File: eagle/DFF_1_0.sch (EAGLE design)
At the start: 15 parts, among them IC1 74HC74N, X1 In A, X2 In B, X3 Ctrl, X4 Out X, X5 Out Y

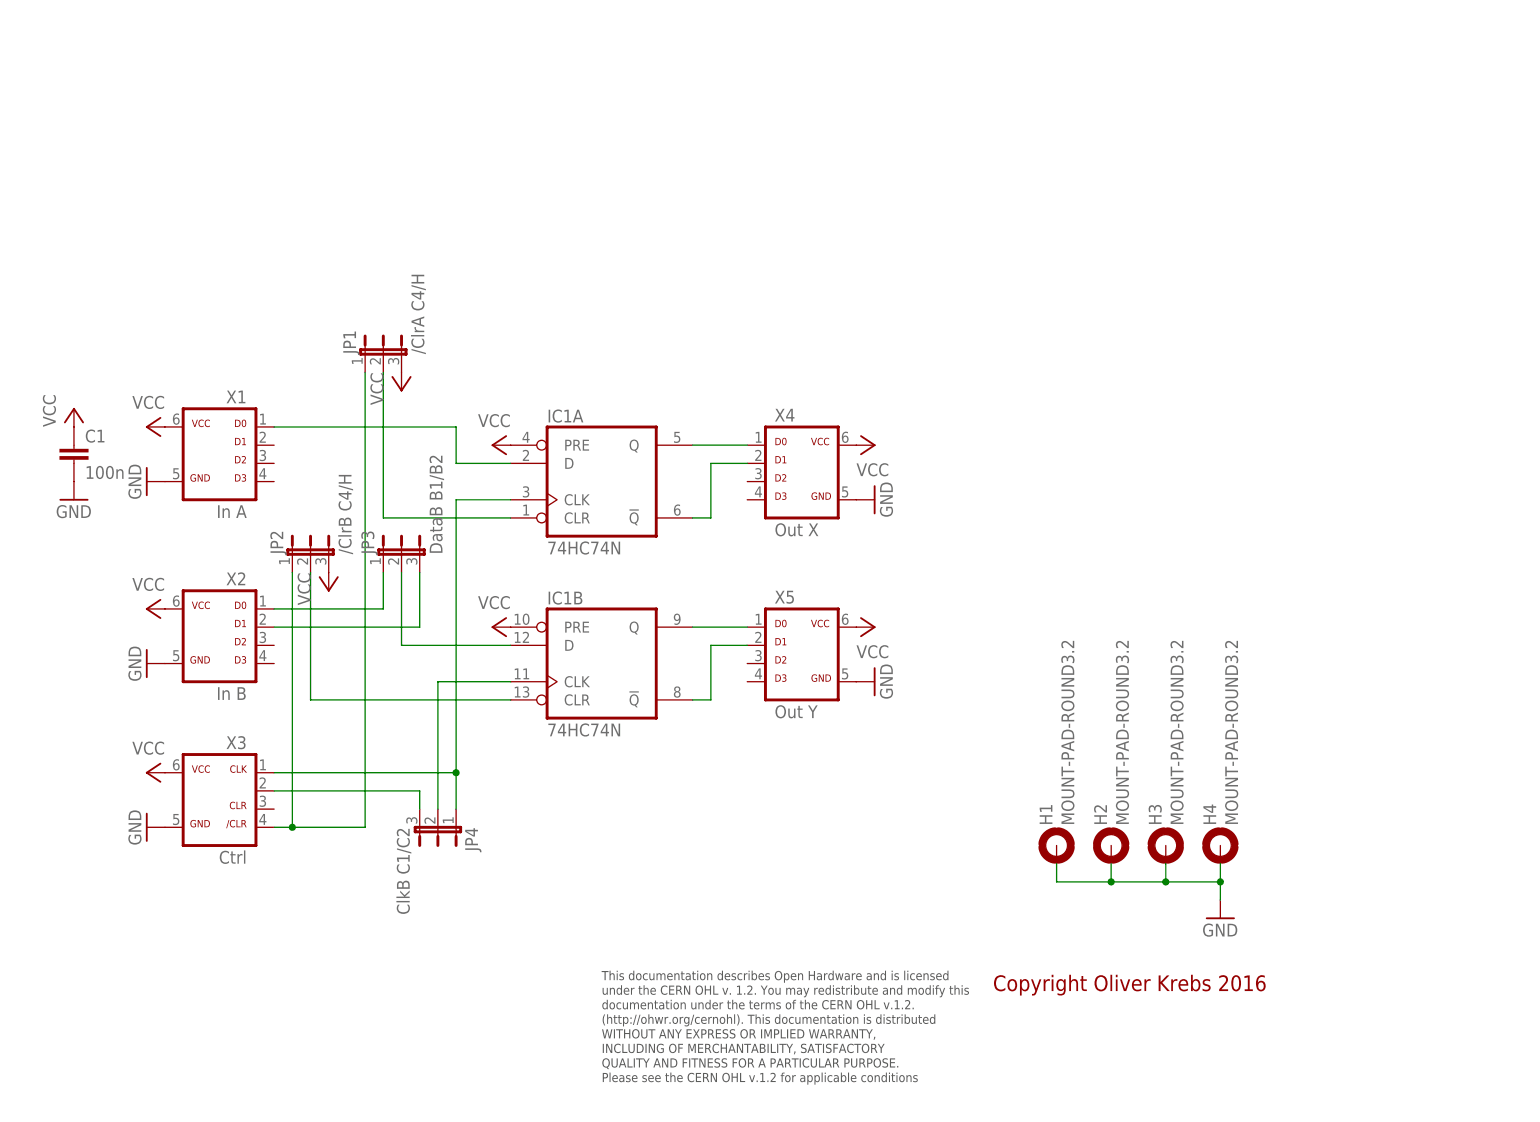
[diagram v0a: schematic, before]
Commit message: Add new tetra-Board and arduino files
Add AMP_1_0, AVC_1_0, D18_1_1, IOP_1_2, MIC_1_0, PIN_1_1, POT_1_0, PWA_1_0, PWR_1_0, RGF 2.0, SOC_2_0, VLT_1_0
Add mex_nano_shield_keyboard, mex_nano_shied_numbers

New arduino projects
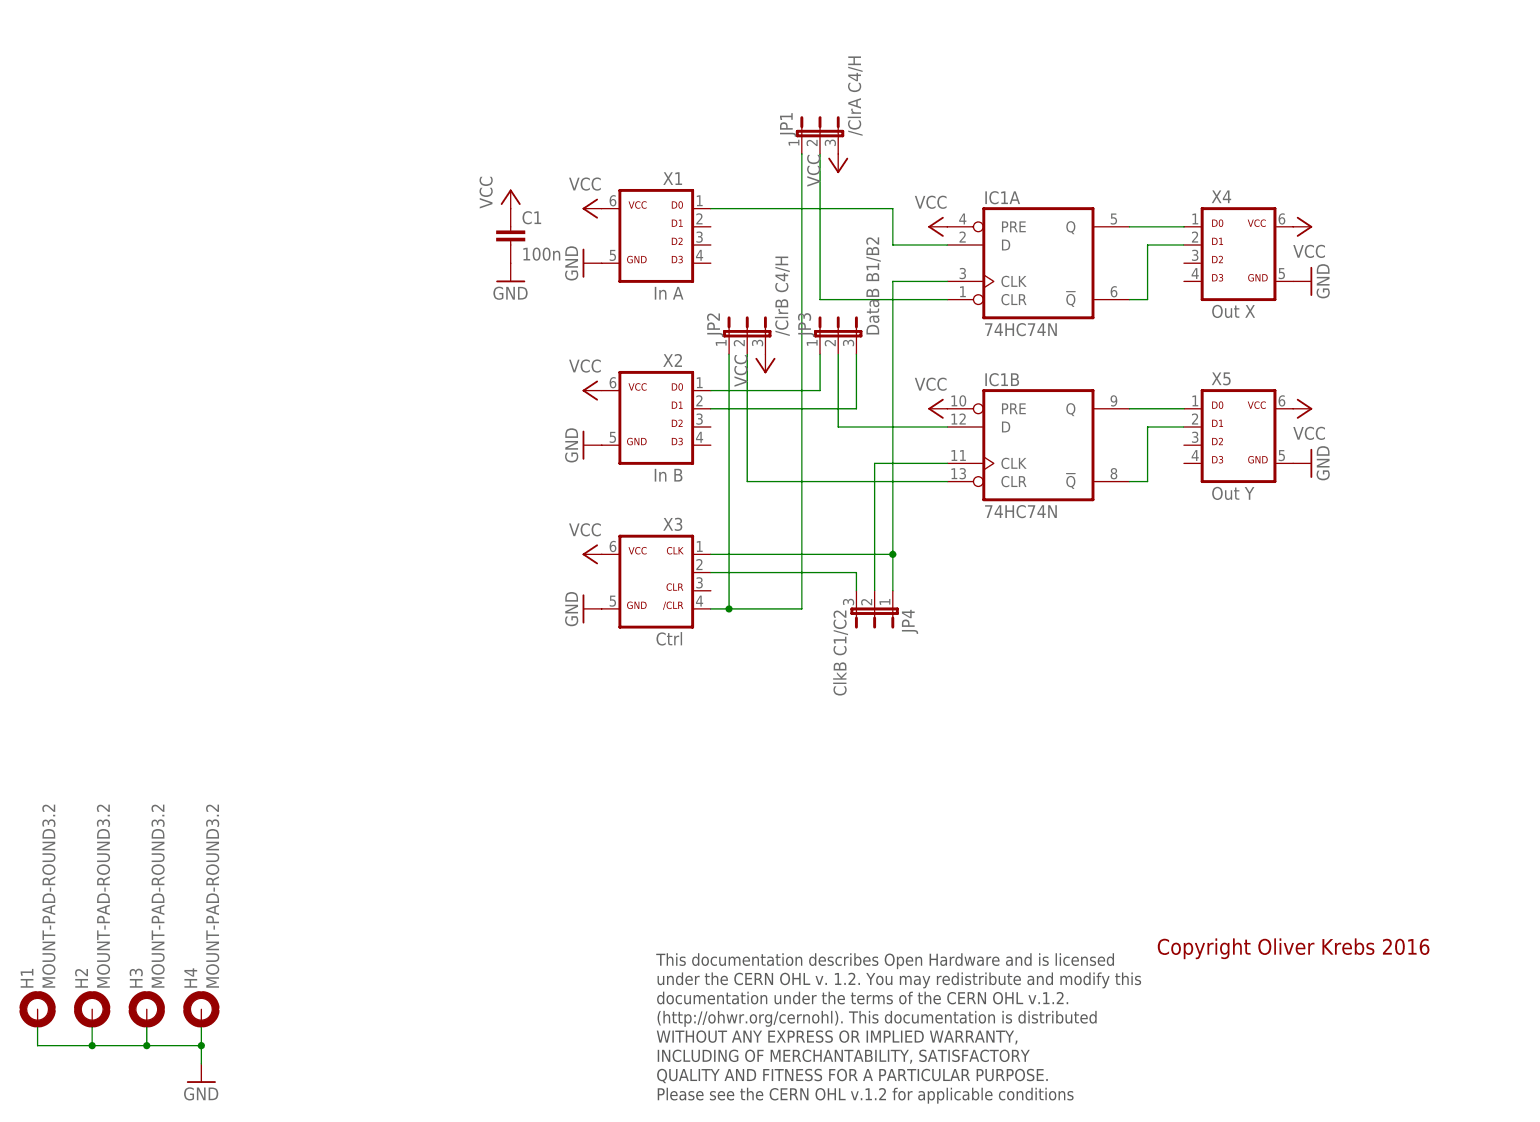
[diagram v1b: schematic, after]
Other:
- moved on the sheet: C1, H1, H2, H3, H4, IC1A, IC1B, JP1, JP2, JP3, JP4, X1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
